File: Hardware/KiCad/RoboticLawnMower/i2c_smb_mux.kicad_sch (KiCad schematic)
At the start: 1 part, among them J13 I2C 0

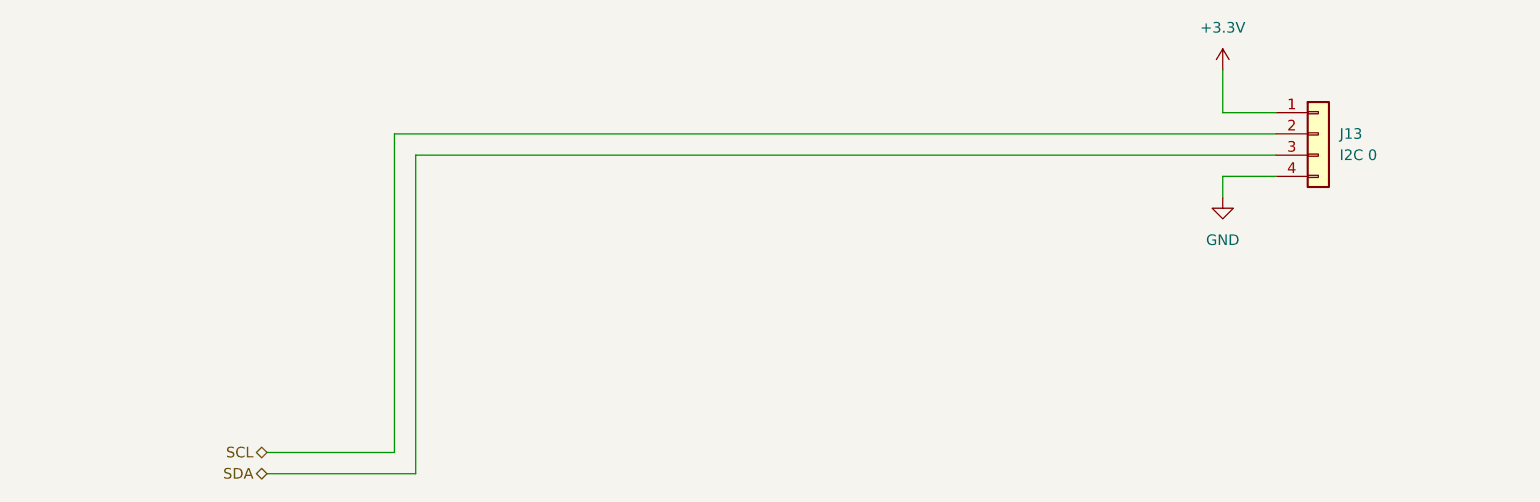
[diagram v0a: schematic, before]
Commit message: Redesign: - Controller - I2C pinning geändert - uvm
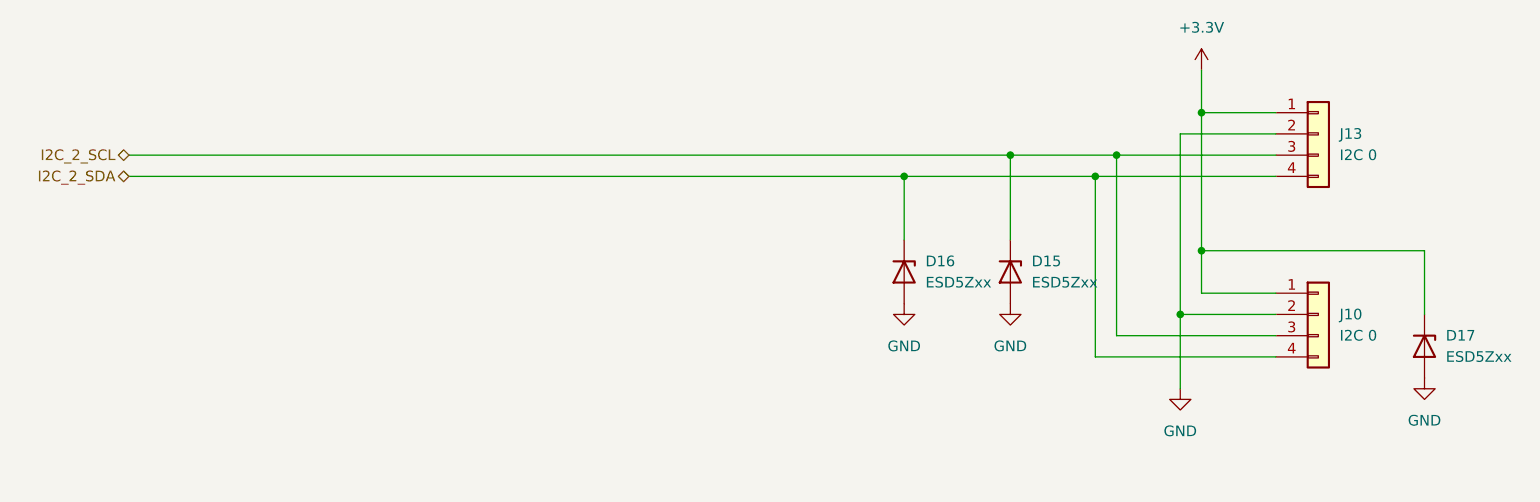
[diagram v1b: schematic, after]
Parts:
- added D15, D16, D17: ESD5Zxx, Diode_SMD:D_SOD-523, symbol Diode:ESD5Zxx
- added J10: I2C 0, Connector_JST:JST_XA_B04B-XASK-1_1x04_P2.50mm_Vertical, symbol Connector_Generic:Conn_01x04
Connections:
- net SCL is gone; now on net GND: J13.2 (Pin_2)
- net +3.3V: now also D17.1 (K), J10.1 (Pin_1)
- net GND: now also D15.2 (A), D16.2 (A), D17.2 (A), J10.2 (Pin_2); no longer J13.4 (Pin_4)
- net SDA renamed I2C_2_SCL
- net I2C_2_SCL: now also D15.1 (K), J10.3 (Pin_3)
- new net I2C_2_SDA: D16.1 (K), J10.4 (Pin_4), J13.4 (Pin_4)
